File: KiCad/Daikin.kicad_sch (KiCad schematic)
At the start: 20 parts, among them J1 SPOX, J2 Prog, Q1 PMF170XP,115, Q2 PMF250XNEX, U1 ESP32-PICO-MINI-02, U2 LMR16006+FB

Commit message: Started reverse engineering
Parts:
- added Q3: PMF250XNEX, Package_TO_SOT_SMD:SOT-323_SC-70, symbol RevK:NX7002AK
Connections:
- net GND: now also Q3.2 (S)
- net RX: now also Q3.3 (D); no longer J1.3 (Pin_3)
- net at Q1.3 (D), Q2.3 (D): now also J1.3 (Pin_3); no longer J1.4 (Pin_4)
- new net: J1.4 (Pin_4), Q3.1 (G)
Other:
- moved on the sheet: J1, J2

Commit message: More
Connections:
- net RX: no longer Q1.2 (S)
- net at J1.4 (Pin_4), Q3.1 (G): now also Q1.2 (S)
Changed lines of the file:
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@@
   (junction (at 147.32 45.72) (diameter 0) (color 0 0 0 0)
+  )
+  (junction (at 129.54 91.44) (diameter 0) (color 0 0 0 0)
   )
   (junction (at 101.6 88.9) (diameter 0) (color 0 0 0 0)
@@
   (no_connect (at 81.28 66.04))
   (no_connect (at 50.8 68.58))
+  (wire (pts (xy 109.22 78.74) (xy 129.54 78.74))
+    (stroke (width 0) (type default) (color 0 0 0 0))
+  )
   (wire (pts (xy 101.6 88.9) (xy 101.6 93.98))
+    (stroke (width 0) (type default) (color 0 0 0 0))
+  )
+  (wire (pts (xy 129.54 78.74) (xy 129.54 91.44))
     (stroke (width 0) (type default) (color 0 0 0 0))
   )
@@
     )
   )
-  (global_label "RX" (shape input) (at 109.22 78.74 90) (fields_autoplaced)
-    (effects (font (size 1.27 1.27)) (justify left))
-    (property "Intersheet References" "${INTERSHEET_REFS}" (id 0) (at 109.1406 73.9363 90)
-      (effects (font (size 1.27 1.27)) (justify left) hide)
-    )
-  )

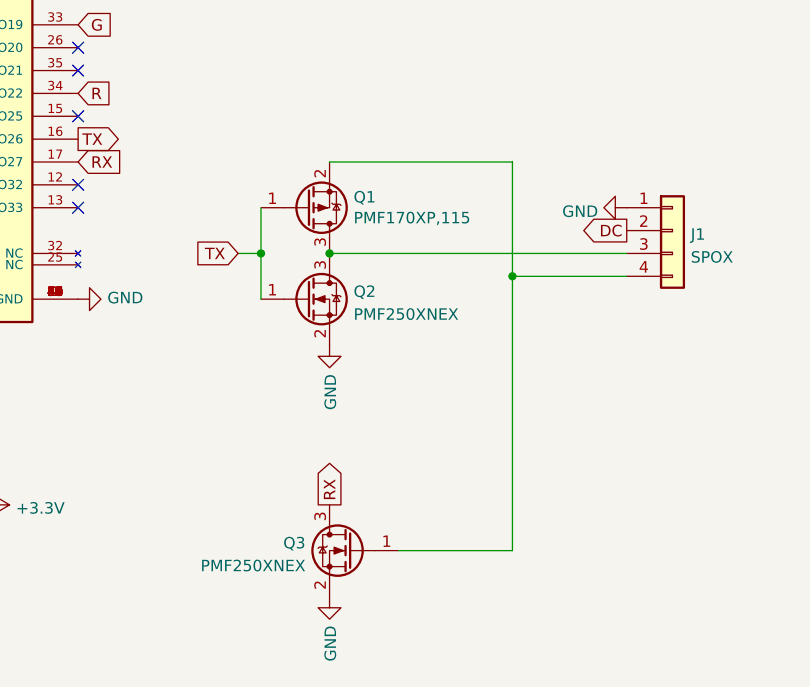
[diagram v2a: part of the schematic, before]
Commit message: Tx will have to be 3.3V, which seems to work OK.
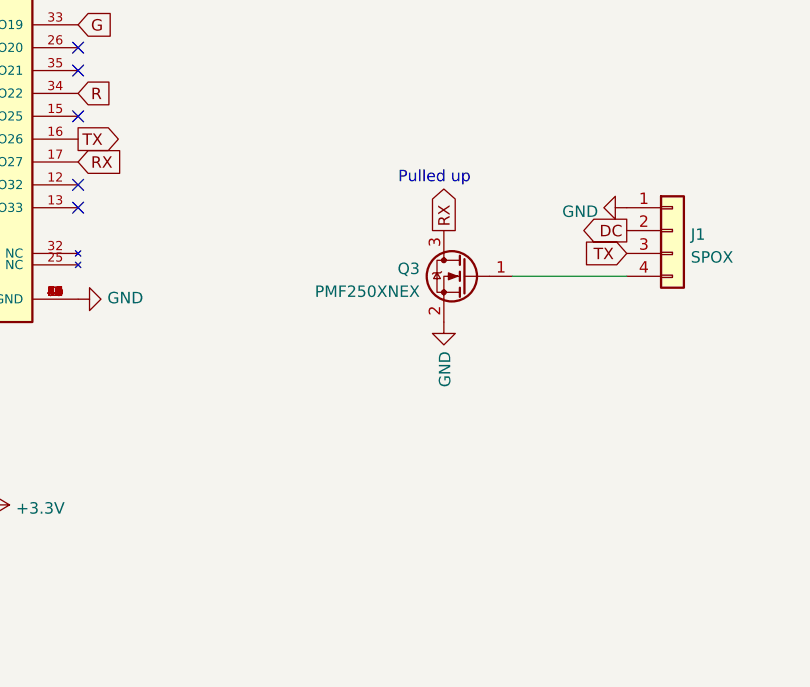
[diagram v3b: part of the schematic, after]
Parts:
- removed Q1: PMF170XP,115, Package_TO_SOT_SMD:SOT-323_SC-70, symbol Device:Q_PMOS_GSD
- removed Q2: PMF250XNEX, Package_TO_SOT_SMD:SOT-323_SC-70, symbol RevK:NX7002AK
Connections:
- net TX: now also J1.3 (Pin_3)
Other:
- note added: "Pulled up"
- moved on the sheet: Q3
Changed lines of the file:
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@@
   (junction (at 147.32 45.72) (diameter 0) (color 0 0 0 0)
   )
-  (junction (at 129.54 91.44) (diameter 0) (color 0 0 0 0)
-  )
-  (junction (at 101.6 88.9) (diameter 0) (color 0 0 0 0)
-  )
   (junction (at 50.8 27.94) (diameter 0) (color 0 0 0 0)
-  )
-  (junction (at 109.22 88.9) (diameter 0) (color 0 0 0 0)
   )
   (junction (at 140.97 36.83) (diameter 0) (color 0 0 0 0)
@@
   (no_connect (at 81.28 66.04))
   (no_connect (at 50.8 68.58))
-  (wire (pts (xy 109.22 78.74) (xy 129.54 78.74))
-    (stroke (width 0) (type default) (color 0 0 0 0))
-  )
-  (wire (pts (xy 101.6 88.9) (xy 101.6 93.98))
-    (stroke (width 0) (type default) (color 0 0 0 0))
-  )
-  (wire (pts (xy 129.54 78.74) (xy 129.54 91.44))
-    (stroke (width 0) (type default) (color 0 0 0 0))
-  )
   (wire (pts (xy 142.24 91.44) (xy 129.54 91.44))
     (stroke (width 0) (type default) (color 0 0 0 0))
   )
-  (wire (pts (xy 129.54 91.44) (xy 129.54 121.92))
-    (stroke (width 0) (type default) (color 0 0 0 0))
-  )
   (wire (pts (xy 140.97 35.56) (xy 140.97 36.83))
     (stroke (width 0) (type default) (color 0 0 0 0))
@@
     (stroke (width 0) (type default) (color 0 0 0 0))
   )
-  (wire (pts (xy 101.6 83.82) (xy 101.6 88.9))
-    (stroke (width 0) (type default) (color 0 0 0 0))
-  )
   (wire (pts (xy 140.97 36.83) (xy 140.97 38.1))
     (stroke (width 0) (type default) (color 0 0 0 0))
@@
     (stroke (width 0) (type default) (color 0 0 0 0))
   )
-  (wire (pts (xy 116.84 121.92) (xy 129.54 121.92))
-    (stroke (width 0) (type default) (color 0 0 0 0))
-  )
   (wire (pts (xy 50.8 27.94) (xy 60.96 27.94))
     (stroke (width 0) (type default) (color 0 0 0 0))
   )
-  (wire (pts (xy 99.06 88.9) (xy 101.6 88.9))
-    (stroke (width 0) (type default) (color 0 0 0 0))
-  )
-  (wire (pts (xy 109.22 88.9) (xy 142.24 88.9))
-    (stroke (width 0) (type default) (color 0 0 0 0))
-  )
   (wire (pts (xy 136.525 40.64) (xy 147.32 40.64))
     (stroke (width 0) (type default) (color 0 0 0 0))
@@
   (wire (pts (xy 140.97 38.1) (xy 147.32 38.1))
     (stroke (width 0) (type default) (color 0 0 0 0))
+  )
+  (text "Pulled up" (at 116.84 81.28 0)
+    (effects (font (size 1.27 1.27)) (justify left bottom))
   )
   (global_label "DC" (shape input) (at 136.525 36.83 180) (fields_autoplaced)
@@
     )
   )
-  (global_label "TX" (shape input) (at 99.06 88.9 180) (fields_autoplaced)
-    (effects (font (size 1.27 1.27)) (justify right))
-    (property "Intersheet References" "${INTERSHEET_REFS}" (id 0) (at 94.5587 88.8206 0)
+  (global_label "TX" (shape input) (at 142.24 88.9 180) (fields_autoplaced)
+    (effects (font (size 1.27 1.27)) (justify right))
+    (property "Intersheet References" "${INTERSHEET_REFS}" (id 0) (at 137.7387 88.8206 0)
       (effects (font (size 1.27 1.27)) (justify right) hide)
     )
@@
     )
   )
-  (global_label "RX" (shape output) (at 109.22 116.84 90) (fields_autoplaced)
+  (global_label "RX" (shape output) (at 121.92 86.36 90) (fields_autoplaced)
     (effects (font (size 1.27 1.27)) (justify left))
-    (property "Intersheet References" "${INTERSHEET_REFS}" (id 0) (at 109.1406 112.0363 90)
+    (property "Intersheet References" "${INTERSHEET_REFS}" (id 0) (at 121.8406 81.5563 90)
       (effects (font (size 1.27 1.27)) (justify left) hide)
     )
@@
     (pin "2")
   )
-  (symbol (lib_id "power:GND") (at 109.22 99.06 0) (unit 1)
-    (in_bom yes) (on_board yes)
-    (property "Reference" "#PWR05" (id 0) (at 109.22 105.41 0)
-      (effects (font (size 1.27 1.27)) hide)
-    )
-    (property "Value" "GND" (id 1) (at 109.347 102.3112 90)
-      (effects (font (size 1.27 1.27)) (justify right))
-    )
-    (property "Footprint" "" (id 2) (at 109.22 99.06 0)
-      (effects (font (size 1.27 1.27)) hide)
-    )
-    (property "Datasheet" "" (id 3) (at 109.22 99.06 0)
-      (effects (font (size 1.27 1.27)) hide)
-    )
-    (pin "1")
-  )
   (symbol (lib_id "power:+3.3V") (at 71.12 116.84 270) (unit 1)
     (in_bom yes) (on_board yes)
@@
     )
     (pin "1")
-  )
-  (symbol (lib_id "Device:Q_PMOS_GSD") (at 106.68 83.82 0) (mirror x) (unit 1)
-    (in_bom yes) (on_board yes)
-    (property "Reference" "Q1" (id 0) (at 111.887 82.6516 0)
-      (effects (font (size 1.27 1.27)) (justify left))
-    )
-    (property "Value" "PMF170XP,115" (id 1) (at 111.887 84.963 0)
-      (effects (font (size 1.27 1.27)) (justify left))
-    )
-    (property "Footprint" "Package_TO_SOT_SMD:SOT-323_SC-70" (id 2) (at 111.76 86.36 0)
-      (effects (font (size 1.27 1.27)) hide)
-    )
-    (property "Datasheet" "~" (id 3) (at 106.68 83.82 0)
-      (effects (font (size 1.27 1.27)) hide)
-    )
-    (property "Note" "Any P-Channel SOT323 that does 3.3V/0.5A" (id 4) (at 106.68 83.82 0)
-      (effects (font (size 1.27 1.27)) hide)
-    )
-    (pin "1")
-    (pin "2")
-    (pin "3")
-  )
-  (symbol (lib_id "RevK:NX7002AK") (at 106.68 93.98 0) (unit 1)
-    (in_bom yes) (on_board yes) (fields_autoplaced)
-    (property "Reference" "Q2" (id 0) (at 111.887 93.1453 0)
-      (effects (font (size 1.27 1.27)) (justify left))
-    )
-    (property "Value" "PMF250XNEX" (id 1) (at 111.887 95.6822 0)
-      (effects (font (size 1.27 1.27)) (justify left))
-    )
-    (property "Footprint" "Package_TO_SOT_SMD:SOT-323_SC-70" (id 2) (at 111.76 91.44 0)
-      (effects (font (size 1.27 1.27)) hide)
-    )
-    (property "Datasheet" "~" (id 3) (at 106.68 93.98 0)
-      (effects (font (size 1.27 1.27)) hide)
-    )
-    (pin "1")
-    (pin "2")
-    (pin "3")
   )
   (symbol (lib_id "Device:R") (at 57.15 116.84 270) (unit 1)
@@
     (pin "2")
   )
-  (symbol (lib_id "power:GND") (at 109.22 127 0) (unit 1)
-    (in_bom yes) (on_board yes)
-    (property "Reference" "#PWR06" (id 0) (at 109.22 133.35 0)
-      (effects (font (size 1.27 1.27)) hide)
-    )
-    (property "Value" "GND" (id 1) (at 109.347 130.2512 90)
-      (effects (font (size 1.27 1.27)) (justify right))
-    )
-    (property "Footprint" "" (id 2) (at 109.22 127 0)
-      (effects (font (size 1.27 1.27)) hide)
-    )
-    (property "Datasheet" "" (id 3) (at 109.22 127 0)
+  (symbol (lib_id "power:GND") (at 121.92 96.52 0) (unit 1)
+    (in_bom yes) (on_board yes)
+    (property "Reference" "#PWR06" (id 0) (at 121.92 102.87 0)
+      (effects (font (size 1.27 1.27)) hide)
+    )
+    (property "Value" "GND" (id 1) (at 122.047 99.7712 90)
+      (effects (font (size 1.27 1.27)) (justify right))
+    )
+    (property "Footprint" "" (id 2) (at 121.92 96.52 0)
+      (effects (font (size 1.27 1.27)) hide)
+    )
+    (property "Datasheet" "" (id 3) (at 121.92 96.52 0)
       (effects (font (size 1.27 1.27)) hide)
     )
@@
     (pin "1")
   )
-  (symbol (lib_id "RevK:NX7002AK") (at 111.76 121.92 0) (mirror y) (unit 1)
-    (in_bom yes) (on_board yes) (fields_autoplaced)
-    (property "Reference" "Q3" (id 0) (at 106.553 121.0853 0)
-      (effects (font (size 1.27 1.27)) (justify left))
-    )
-    (property "Value" "PMF250XNEX" (id 1) (at 106.553 123.6222 0)
-      (effects (font (size 1.27 1.27)) (justify left))
-    )
-    (property "Footprint" "Package_TO_SOT_SMD:SOT-323_SC-70" (id 2) (at 106.68 119.38 0)
-      (effects (font (size 1.27 1.27)) hide)
-    )
-    (property "Datasheet" "~" (id 3) (at 111.76 121.92 0)
+  (symbol (lib_id "RevK:NX7002AK") (at 124.46 91.44 0) (mirror y) (unit 1)
+    (in_bom yes) (on_board yes) (fields_autoplaced)
+    (property "Reference" "Q3" (id 0) (at 119.253 90.6053 0)
+      (effects (font (size 1.27 1.27)) (justify left))
+    )
+    (property "Value" "PMF250XNEX" (id 1) (at 119.253 93.1422 0)
+      (effects (font (size 1.27 1.27)) (justify left))
+    )
+    (property "Footprint" "Package_TO_SOT_SMD:SOT-323_SC-70" (id 2) (at 119.38 88.9 0)
+      (effects (font (size 1.27 1.27)) hide)
+    )
+    (property "Datasheet" "~" (id 3) (at 124.46 91.44 0)
       (effects (font (size 1.27 1.27)) hide)
     )
@@
       (reference "#PWR04") (unit 1) (value "GND") (footprint "")
     )
-    (path "/2d993015-d3ce-42f4-af47-fba3fb5e90d6"
-      (reference "#PWR05") (unit 1) (value "GND") (footprint "")
-    )
     (path "/e81930cd-ec3d-4f39-b139-4cba4f23d7a3"
       (reference "#PWR06") (unit 1) (value "GND") (footprint "")
@@
       (reference "L1") (unit 1) (value "6.8uH") (footprint "RevK:Hidden")
     )
-    (path "/60333601-99f6-42aa-8c36-287814730d80"
-      (reference "Q1") (unit 1) (value "PMF170XP,115") (footprint "Package_TO_SOT_SMD:SOT-323_SC-70")
-    )
-    (path "/71c7be27-c495-456d-8161-4660f57b8dd8"
-      (reference "Q2") (unit 1) (value "PMF250XNEX") (footprint "Package_TO_SOT_SMD:SOT-323_SC-70")
-    )
     (path "/ebcfdf36-110d-4f79-9de0-e4fcd76c1d6e"

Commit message: PCb design
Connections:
- net G: now also U1.28 (IO8); no longer U1.33 (IO19)
- net R: now also U1.33 (IO19); no longer U1.34 (IO22)
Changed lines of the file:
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@@
   (junction (at 136.525 43.18) (diameter 0) (color 0 0 0 0)
   )
-  (no_connect (at 50.8 76.2))
+  (no_connect (at 81.28 71.12))
   (no_connect (at 50.8 45.72))
   (no_connect (at 50.8 48.26))
@@
     )
   )
-  (global_label "G" (shape input) (at 81.28 63.5 0) (fields_autoplaced)
-    (effects (font (size 1.27 1.27)) (justify left))
-    (property "Intersheet References" "${INTERSHEET_REFS}" (id 0) (at 184.15 163.83 0)
+  (global_label "G" (shape input) (at 50.8 76.2 180) (fields_autoplaced)
+    (effects (font (size 1.27 1.27)) (justify right))
+    (property "Intersheet References" "${INTERSHEET_REFS}" (id 0) (at -52.07 -24.13 0)
       (effects (font (size 1.27 1.27)) hide)
     )
   )
-  (global_label "R" (shape input) (at 81.28 71.12 0) (fields_autoplaced)
+  (global_label "R" (shape input) (at 81.28 63.5 0) (fields_autoplaced)
     (effects (font (size 1.27 1.27)) (justify left))
-    (property "Intersheet References" "${INTERSHEET_REFS}" (id 0) (at 184.15 166.37 0)
+    (property "Intersheet References" "${INTERSHEET_REFS}" (id 0) (at 184.15 158.75 0)
       (effects (font (size 1.27 1.27)) hide)
     )

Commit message: Tweak prog
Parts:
- J2: footprint Connector_PinHeader_2.54mm:PinHeader_1x05_P2.54mm_Vertical -> RevK:Shelly; symbol Connector_Generic:Conn_01x05 -> RevK:Shelly; now in the parts list
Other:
- moved on the sheet: J2
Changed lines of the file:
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@@
     (pin "3")
   )
-  (symbol (lib_id "Connector_Generic:Conn_01x05") (at 198.12 86.36 0) (unit 1)
-    (in_bom no) (on_board yes)
+  (symbol (lib_id "RevK:Shelly") (at 198.12 86.36 0) (unit 1)
+    (in_bom yes) (on_board yes)
     (property "Reference" "J2" (id 0) (at 196.85 77.47 0)
       (effects (font (size 1.27 1.27)) (justify left))
     )
-    (property "Value" "Prog" (id 1) (at 200.025 86.36 0)
+    (property "Value" "Prog" (id 1) (at 198.12 96.52 0)
       (effects (font (size 1.27 1.27)) (justify left))
     )
-    (property "Footprint" "Connector_PinHeader_2.54mm:PinHeader_1x05_P2.54mm_Vertical" (id 2) (at 198.12 93.98 0)
+    (property "Footprint" "RevK:Shelly" (id 2) (at 198.12 95.25 0)
       (effects (font (size 1.27 1.27)) hide)
     )
-    (property "Datasheet" "~" (id 3) (at 198.12 86.36 0)
+    (property "Datasheet" "~" (id 3) (at 198.12 95.25 0)
       (effects (font (size 1.27 1.27)) hide)
     )
@@
     )
     (path "/ee567585-ddb7-4c4a-a692-94261f4c4bce"
-      (reference "J2") (unit 1) (value "Prog") (footprint "Connector_PinHeader_2.54mm:PinHeader_1x05_P2.54mm_Vertical")
+      (reference "J2") (unit 1) (value "Prog") (footprint "RevK:Shelly")
     )
     (path "/00000000-0000-0000-0000-0000610fe01a"
